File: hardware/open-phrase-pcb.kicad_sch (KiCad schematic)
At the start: 5 parts, among them J1 Conn_01x36, J2 Conn_01x36, J3 Conn_01x36, J4 Conn_01x36

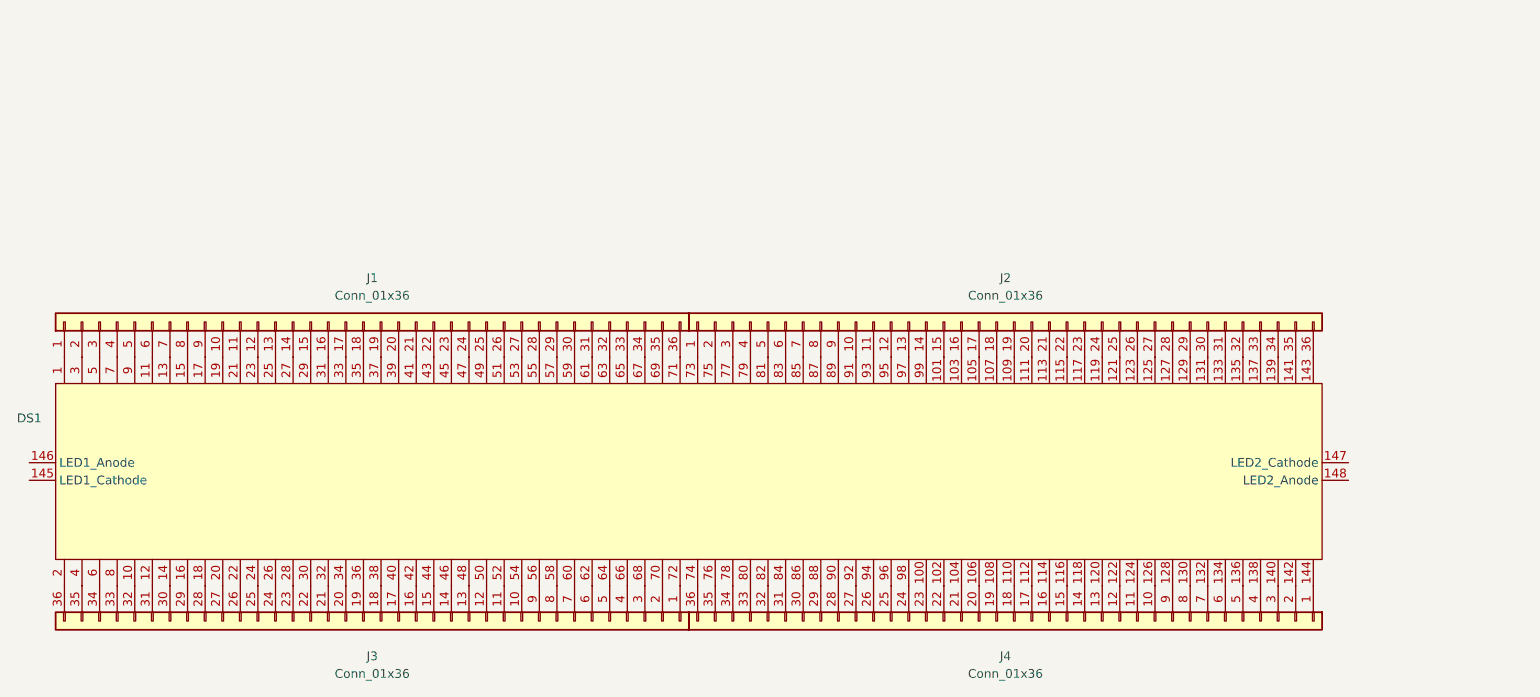
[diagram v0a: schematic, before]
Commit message: Replicated PCB layout
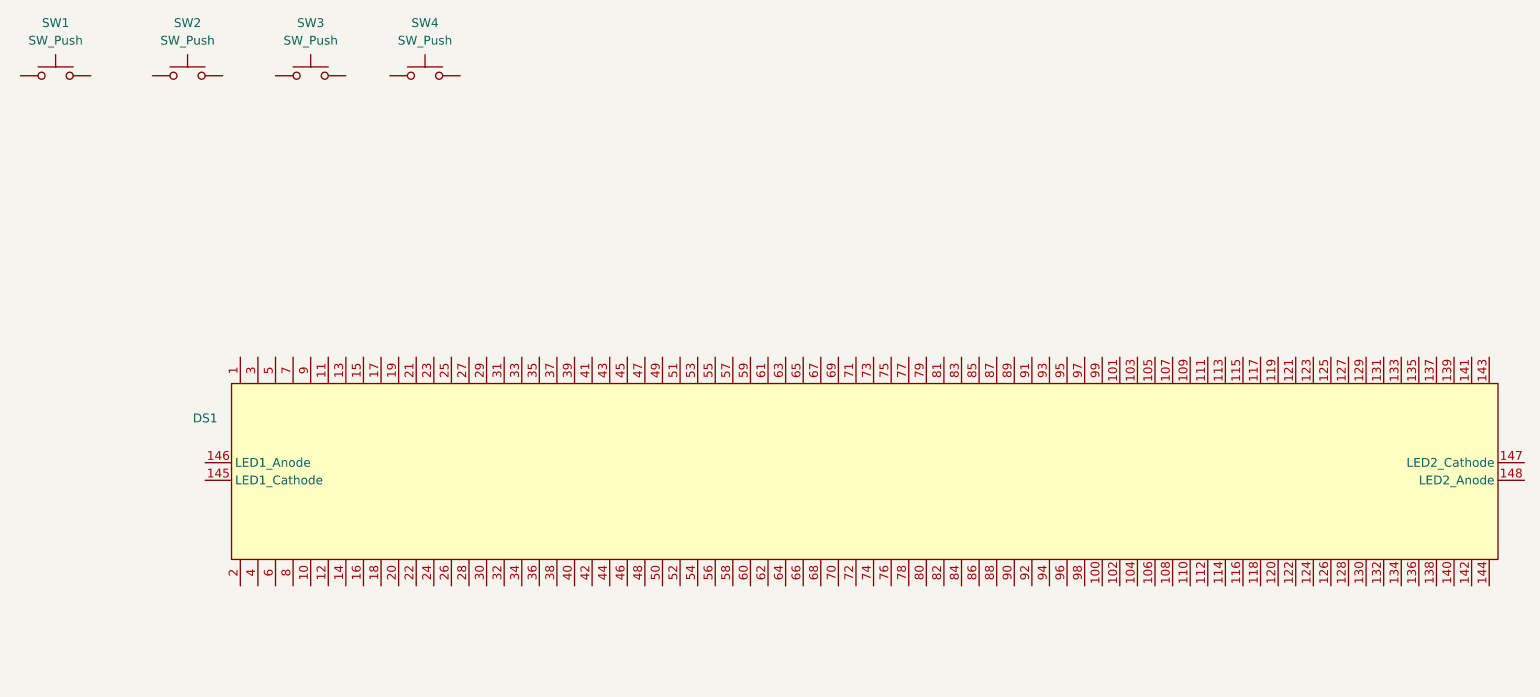
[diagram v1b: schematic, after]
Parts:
- removed J1, J2, J3, J4: Conn_01x36, Connector_PinHeader_1.00mm:PinHeader_1x36_P1.00mm_Vertical, symbol Connector_Generic:Conn_01x36
- added SW1, SW2, SW3, SW4: SW_Push, custom-components:Switch_Pad_5x5mm_CaptiveMembrane_2x2mm_9mm, symbol Switch:SW_Push
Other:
- moved on the sheet: DS1
